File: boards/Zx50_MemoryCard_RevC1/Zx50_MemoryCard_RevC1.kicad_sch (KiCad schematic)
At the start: 49 parts, among them J3 Zx50_EdgeConnector, J4 TP_CLK, J5 TP_MCLK, Q1 2N7002, SW1 SW_DIP_x05, U10 74LVC3G07, U11 74LVC245, U21 74LVC245, U22 SN74LVC1G17DBVR, U23 74LVC245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

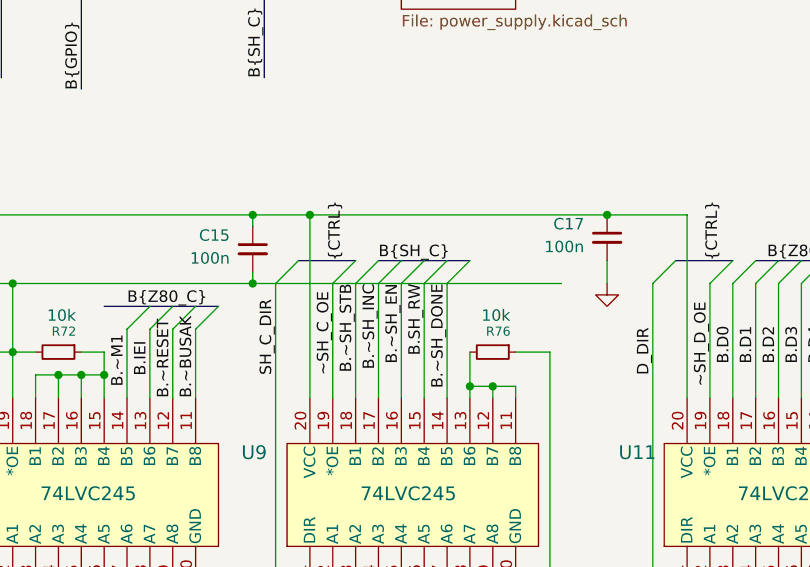
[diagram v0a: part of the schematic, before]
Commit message: fireware fixes for serial card and getting pico-pic async working better.
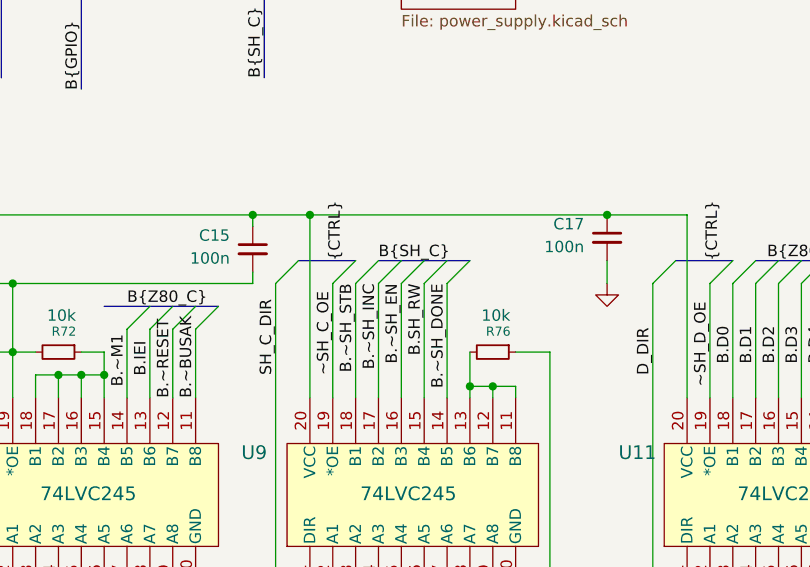
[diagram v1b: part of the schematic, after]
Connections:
- net GND: no longer R3.1, U9.1 (DIR), U9.14 (B5), U9.15 (B4), U9.16 (B3), U9.17 (B2), U9.18 (B1), U9.19 (*OE)
- new net B.SH_RW: U9.15 (B4)
- new net B.~SH_DONE: U9.14 (B5)
- new net B.~SH_EN: U9.16 (B3)
- new net B.~SH_INC: U9.17 (B2)
- new net B.~SH_STB: U9.18 (B1)
- new net SH_C_DIR: U9.1 (DIR)
- new net ~SH_C_OE: R3.1, U9.19 (*OE)
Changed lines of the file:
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@@
 	)
 	(junction
-		(at 201.93 62.23)
-		(diameter 0)
-		(color 0 0 0 0)
-	)
-	(junction
 		(at 27.94 125.73)
 		(diameter 0)
@@
 	(wire
 		(pts
-			(xy 201.93 62.23) (xy 204.47 62.23)
-		)
-		(stroke
-			(width 0)
-			(type default)
-		)
-	)
-	(wire
-		(pts
 			(xy 55.88 116.84) (xy 50.8 116.84)
 		)
@@
 	(wire
 		(pts
-			(xy 218.44 62.23) (xy 220.98 62.23)
-		)
-		(stroke
-			(width 0)
-			(type default)
-		)
-	)
-	(wire
-		(pts
 			(xy 140.97 120.65) (xy 140.97 121.92)
 		)
@@
 	(wire
 		(pts
-			(xy 204.47 62.23) (xy 210.82 62.23)
-		)
-		(stroke
-			(width 0)
-			(type default)
-		)
-	)
-	(wire
-		(pts
 			(xy 127 68.58) (xy 127 74.93)
 		)
@@
 	(wire
 		(pts
-			(xy 223.52 62.23) (xy 236.22 62.23)
-		)
-		(stroke
-			(width 0)
-			(type default)
-		)
-	)
-	(wire
-		(pts
 			(xy 273.05 62.23) (xy 273.05 74.93)
 		)
@@
 		)
 	)
-	(wire
-		(pts
-			(xy 210.82 62.23) (xy 213.36 62.23)
-		)
-		(stroke
-			(width 0)
-			(type default)
-		)
-	)
 	(bus
 		(pts
@@
 	(wire
 		(pts
-			(xy 220.98 62.23) (xy 223.52 62.23)
-		)
-		(stroke
-			(width 0)
-			(type default)
-		)
-	)
-	(wire
-		(pts
 			(xy 182.88 132.08) (xy 184.15 132.08)
 		)
@@
 		)
 	)
-	(wire
-		(pts
-			(xy 215.9 62.23) (xy 218.44 62.23)
-		)
-		(stroke
-			(width 0)
-			(type default)
-		)
-	)
 	(bus
 		(pts
@@
 		)
 		(stroke
-			(width 0)
-			(type default)
-		)
-	)
-	(wire
-		(pts
-			(xy 213.36 62.23) (xy 215.9 62.23)
-		)
-		(stroke
